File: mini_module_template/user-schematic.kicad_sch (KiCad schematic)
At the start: 19 parts

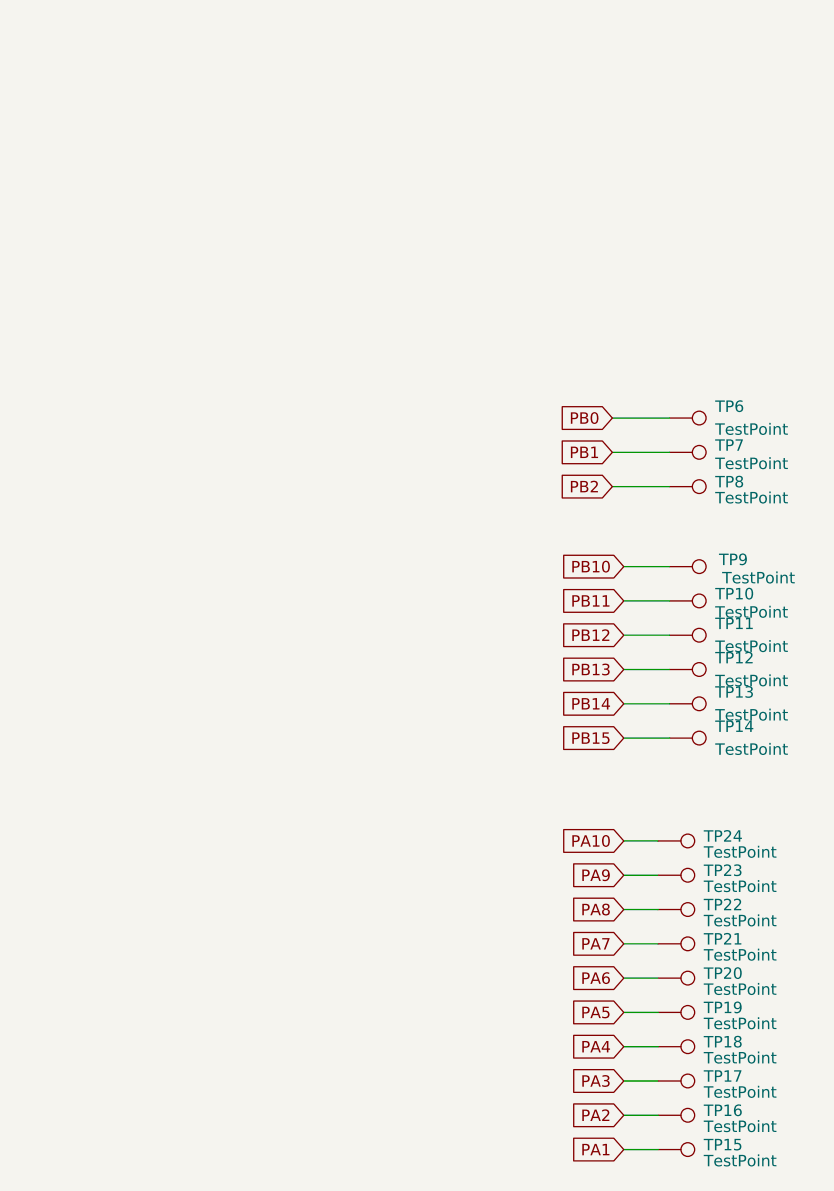
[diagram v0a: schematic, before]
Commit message: revison C, aded 2 can support and gight voltage input stepdown
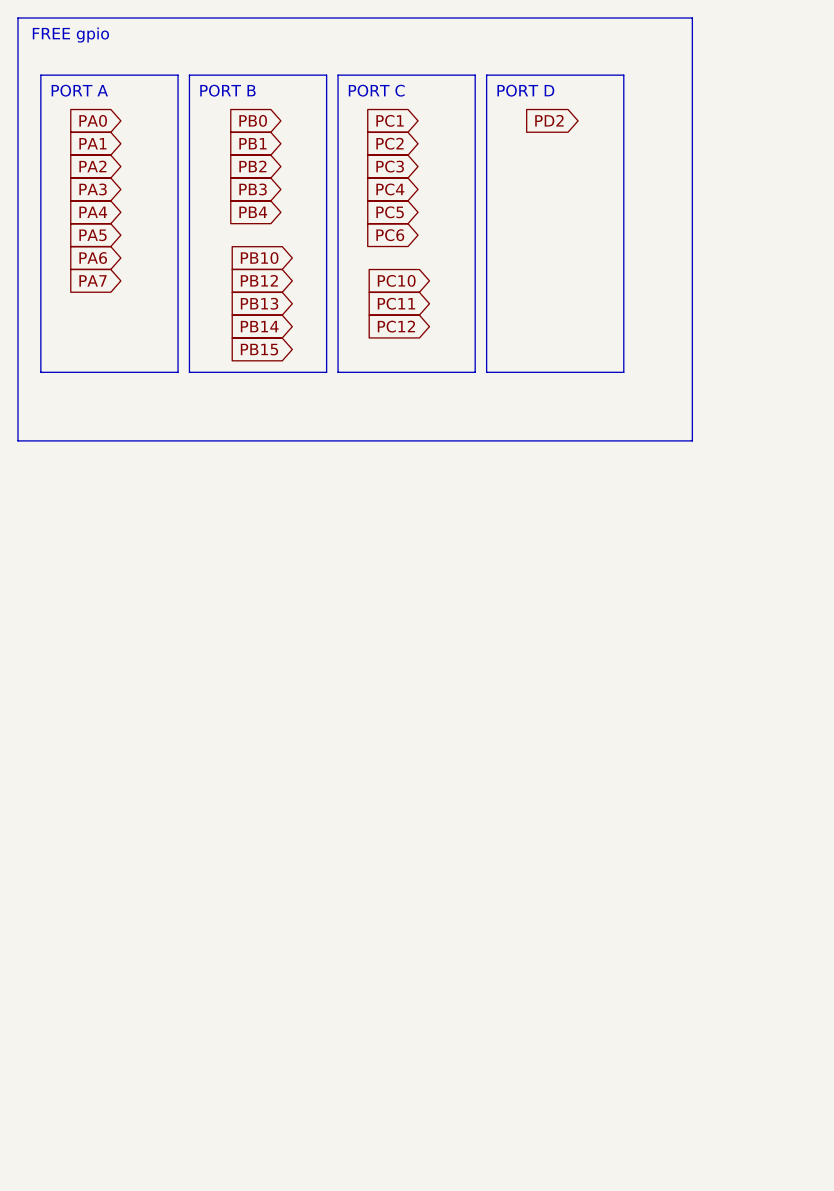
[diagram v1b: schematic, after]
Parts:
- removed TP10, TP11, TP12, TP13, TP14, TP15, TP16, TP17, TP18, TP19, TP20, TP21, TP22, TP23, TP24, TP6, TP7, TP8, TP9: TestPoint, TestPoint:TestPoint_Pad_1.0x1.0mm, symbol Connector:TestPoint
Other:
- note added: "FREE gpio"

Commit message: updaet schematic
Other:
- company: (none) -> Patryk Dudziński
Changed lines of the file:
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@@
 	(generator_version "8.0")
 	(paper "A4")
+	(title_block
+		(date "2025-01-10")
+		(rev "1.0")
+		(company "Patryk Dudziński")
+	)
 	(rectangle
 		(start 19.05 16.51)
